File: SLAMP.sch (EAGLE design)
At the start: 65 parts, among them IC2 AT42QT1070-SSU, J1 CARA1, J2 CARA4, J3 CARA2, J4 CARA5, J5 CARA3, J6 EXTRA-D10, J7 A0, Q1 2N7002PW, Q2 BC548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

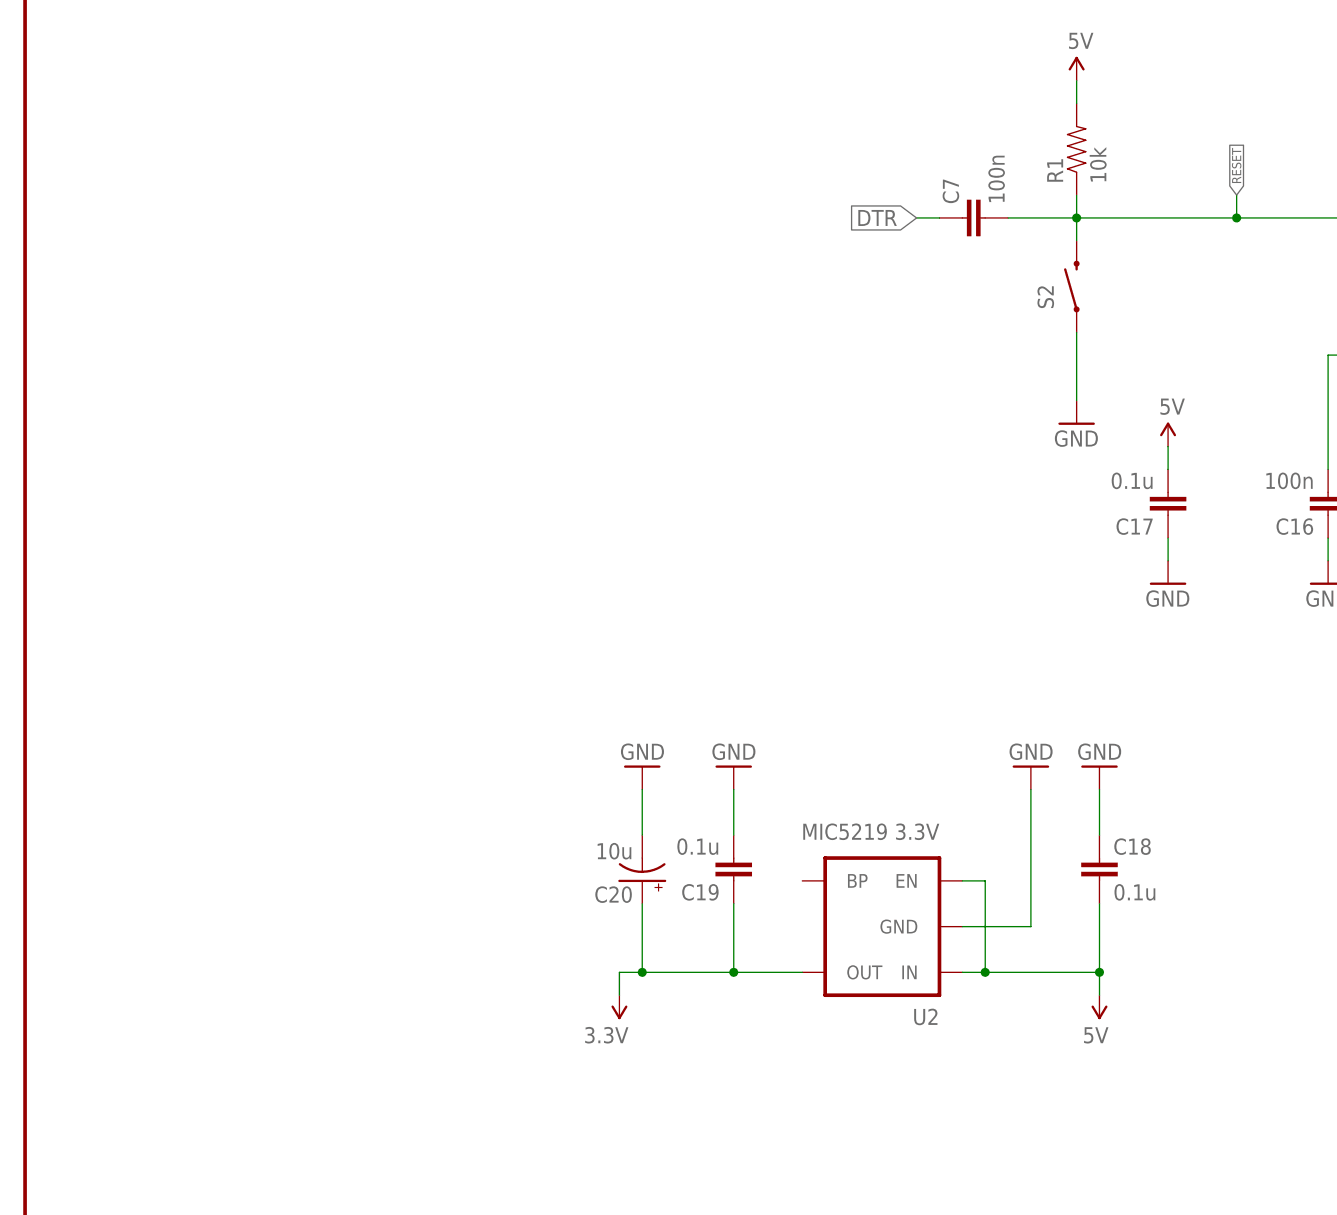
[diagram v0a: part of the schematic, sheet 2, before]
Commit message: Working on the power management
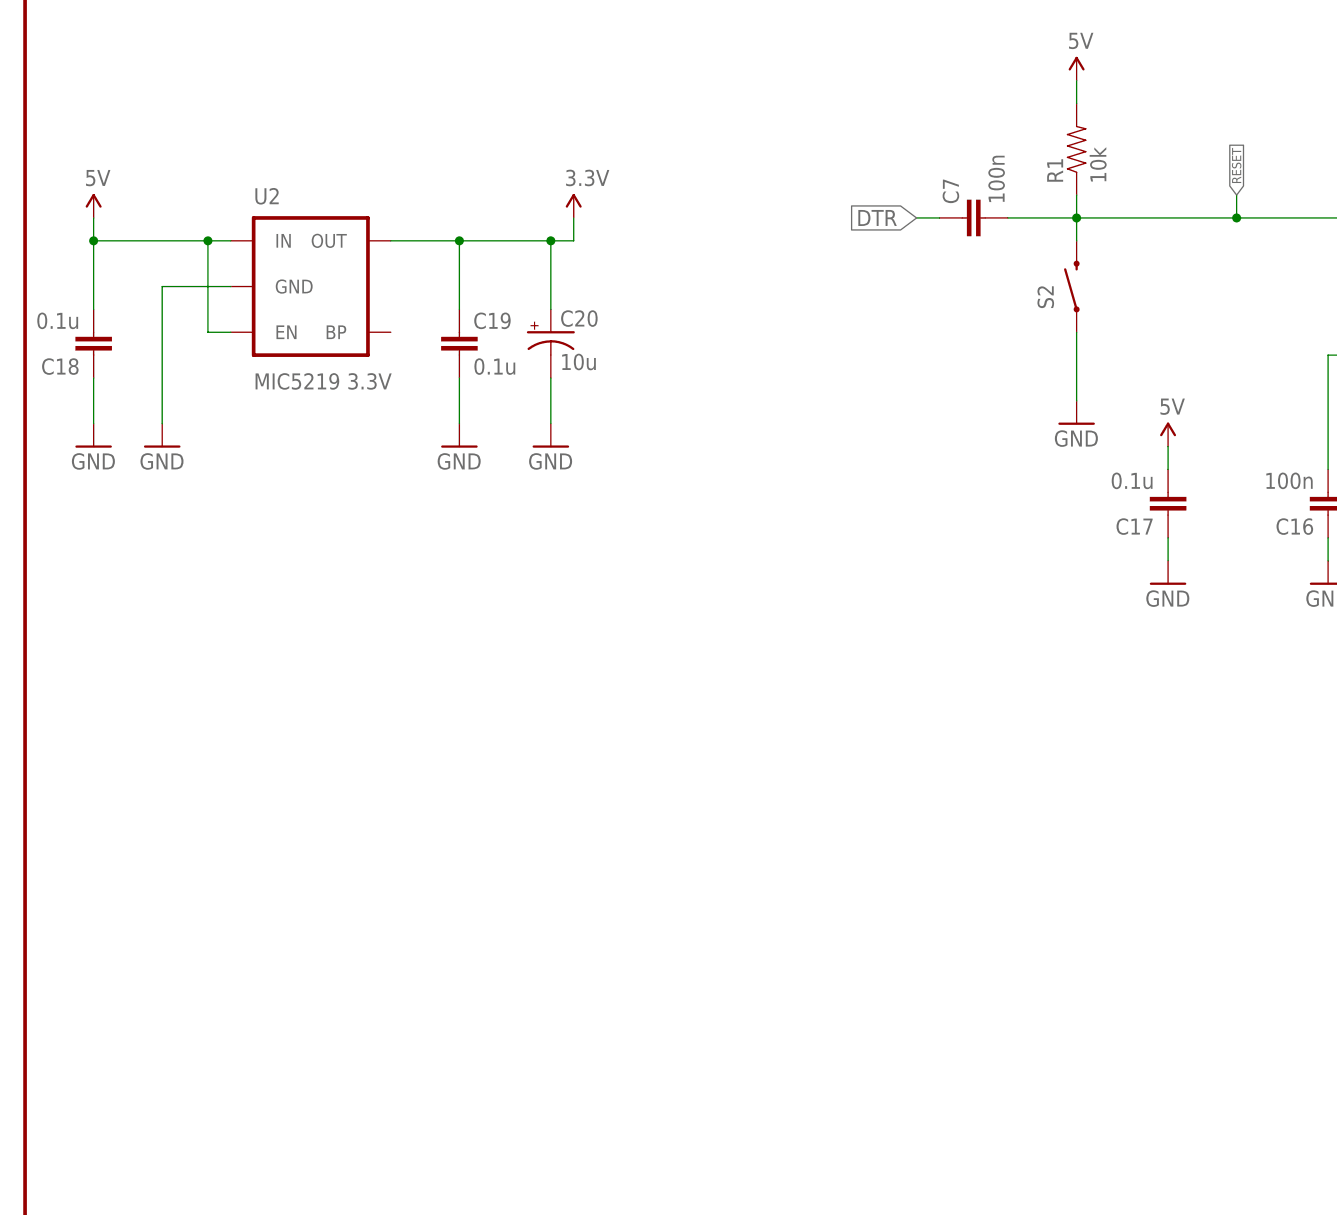
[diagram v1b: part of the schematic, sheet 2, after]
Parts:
- removed C8: 10n, SparkFun-Passives:CAP0603-CAP
- removed D2: PINK, SparkFun-LED:LED-PINK1206
- removed F2: 500mA, SparkFun-PowerIC:PTCSMD
- removed Q2: BC548, transistor-npn:BC548
- removed Q3: IRF520, transistor-power:IRF520
- removed R19, R2, R3: 2k, SparkFun-Passives:RESISTOR0805-RES
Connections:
- removed net N$18: F2.1, JP1.4
- removed net N$22: D2.C, Q3.D
- removed net N$6: Q2.B, R2.2, R3.2
- removed net N$7: Q2.C, Q3.G, R19.2
- removed net VCC_POWERSUPPLY: R2.1
- removed net VUSB: C8.1, D2.A, F2.2
- net 5V: no longer Q3.S, R19.1
- net GND: no longer C8.2, Q2.E, R3.1
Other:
- moved on the sheet: C18, C19, C20, U2

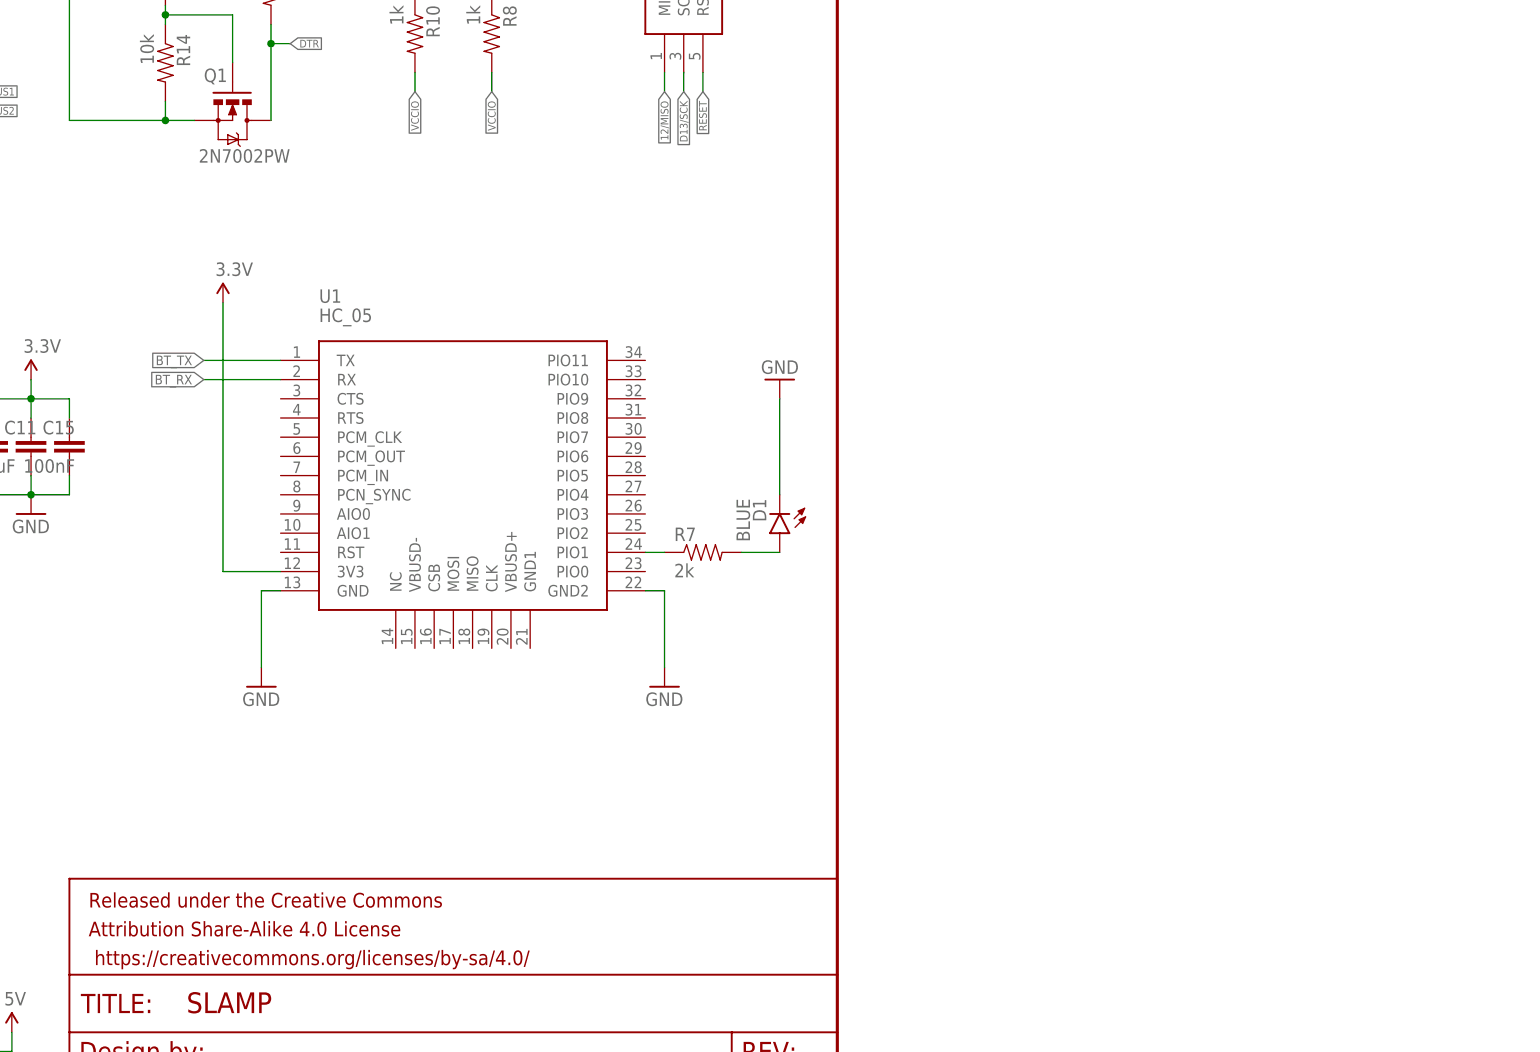
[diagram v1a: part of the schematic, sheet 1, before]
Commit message: Power control finished
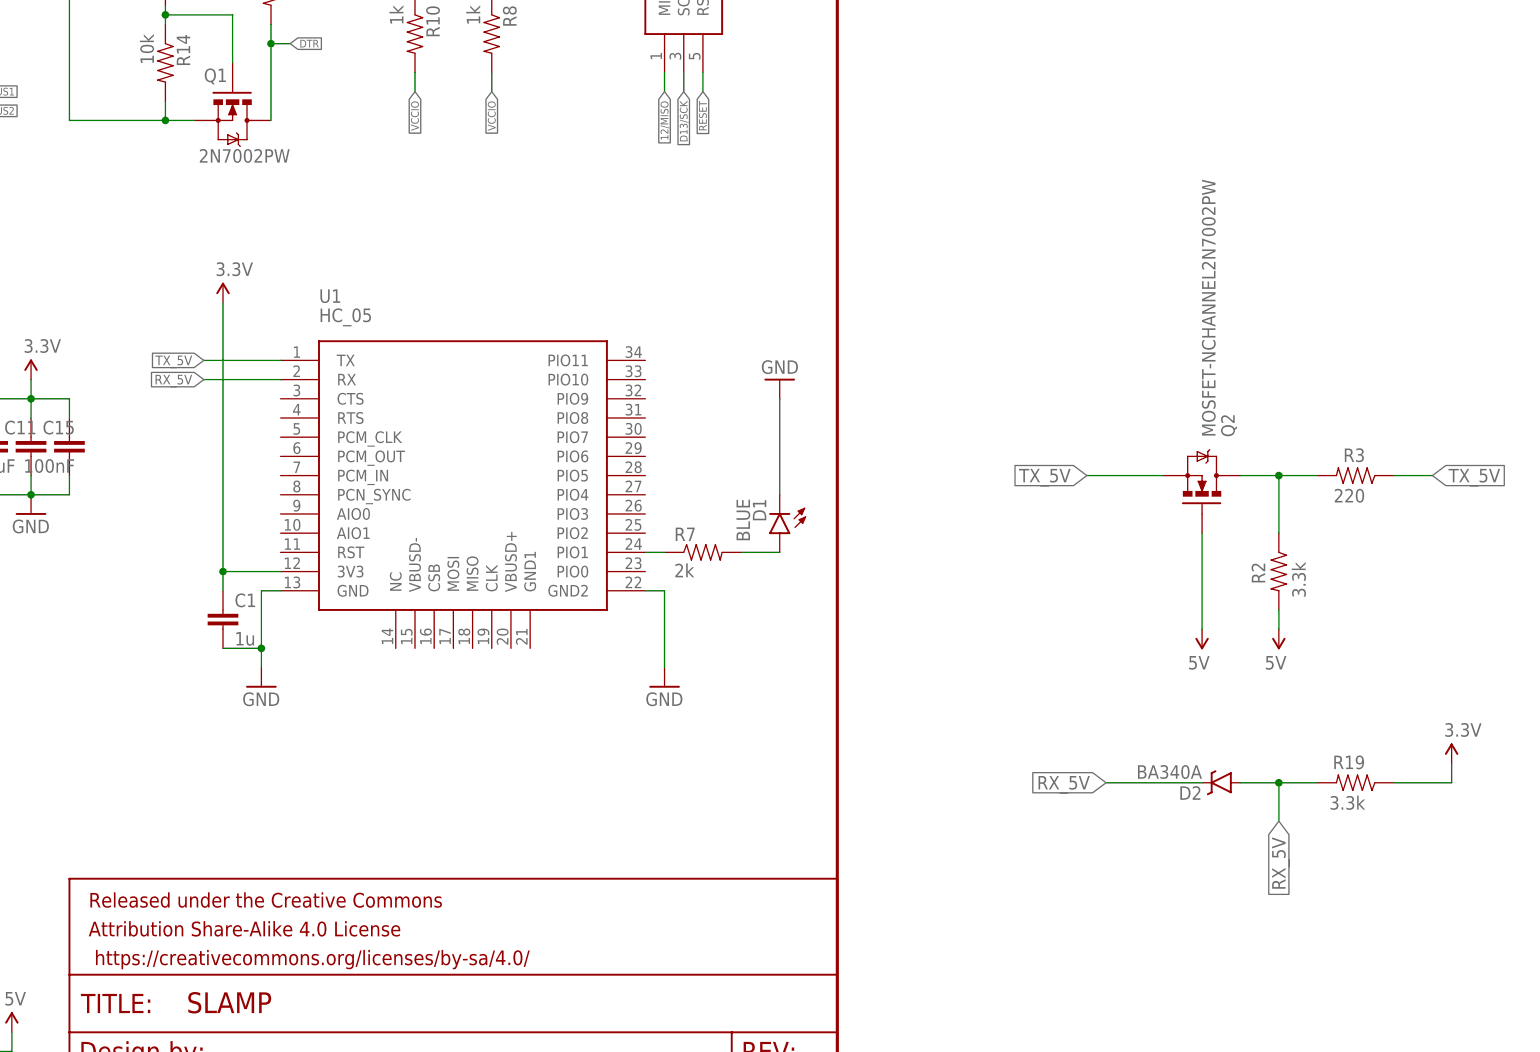
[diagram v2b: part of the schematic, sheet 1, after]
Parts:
- added C1: 1u, SparkFun-Passives:CAP0603-CAP
- added D2: BA340A, SparkFun-DiscreteSemi:B340A
- added Q2: MOSFET-NCHANNEL2N7002PW, SparkFun-DiscreteSemi:MOSFET-NCHANNEL2N7002PW
- added R19, R2: 3.3k, SparkFun-Passives:RESISTOR0603-RES
- added R3: 220, SparkFun-Passives:RESISTOR0603-RES
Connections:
- removed net BT_RX: U1.RX, U3.PD3(INT1)
- removed net BT_TX: U1.TX, U3.PD2(INT0)
- new net N$7: Q2.D, R2.1, R3.2
- new net RX_5V: D2.A, D2.C, R19.2, U1.RX, U3.PD3(INT1)
- new net TX_5V: Q2.S, R3.1, U1.TX, U3.PD2(INT0)
- net 3.3V: now also C1.1, R19.1
- net 5V: now also Q2.G, R2.2
- net GND: now also C1.2
